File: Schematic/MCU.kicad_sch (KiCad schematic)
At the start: 21 parts, among them IC3 STM32H743VIT6, SW1 TS24CA, Y1 8MHz

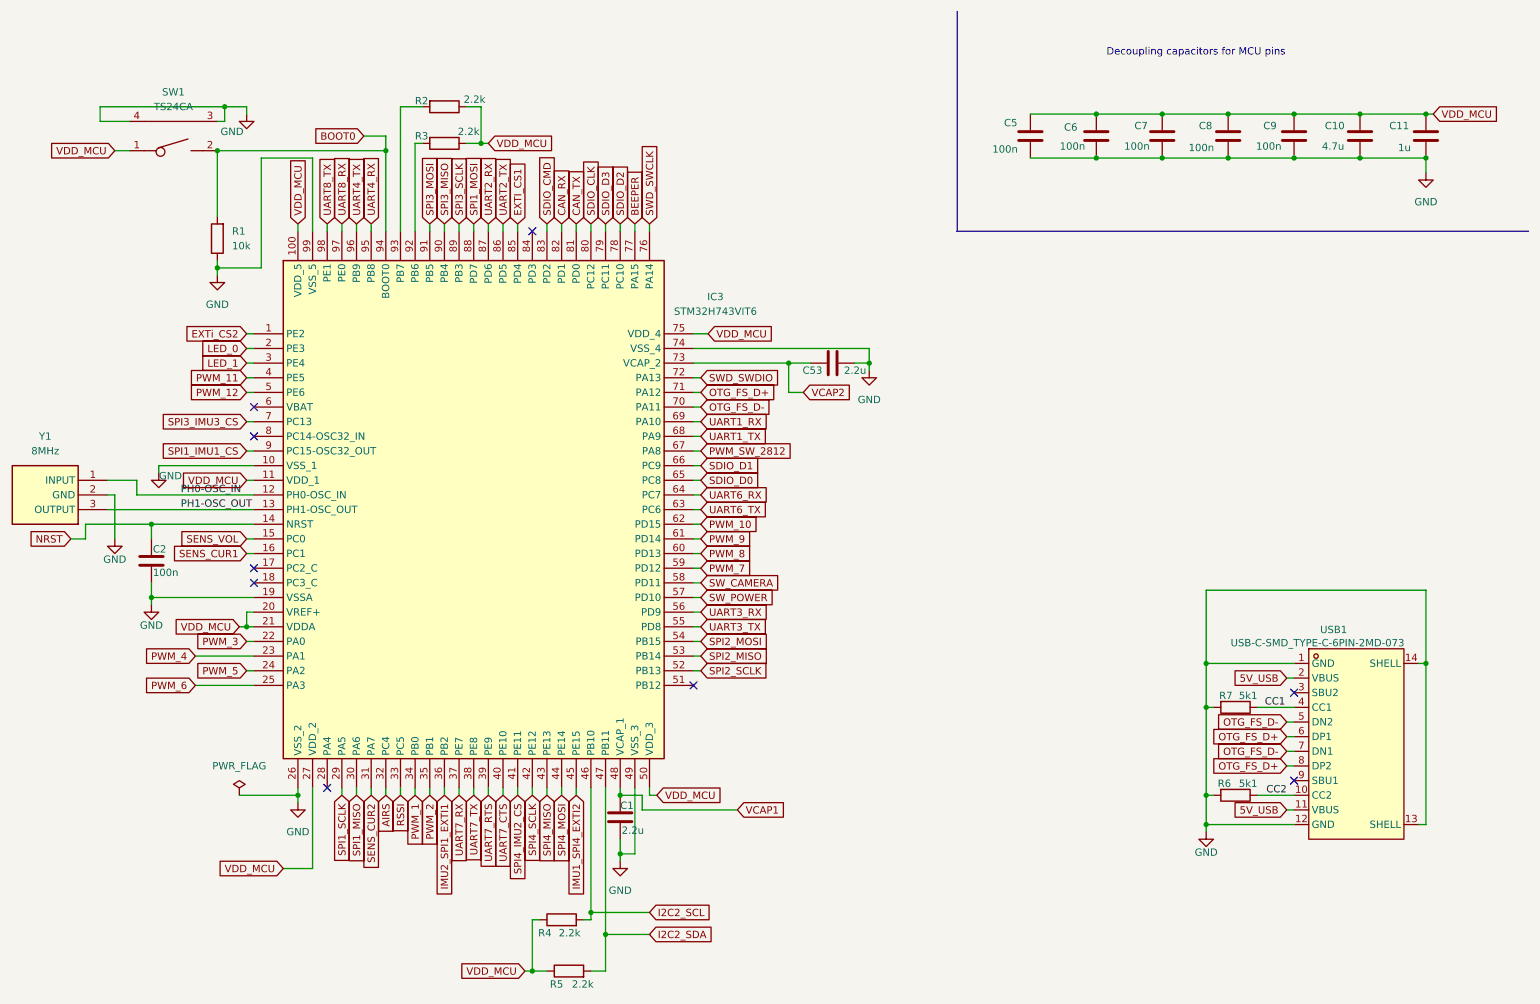
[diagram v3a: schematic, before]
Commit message: still routing and defining plan zones for power nets
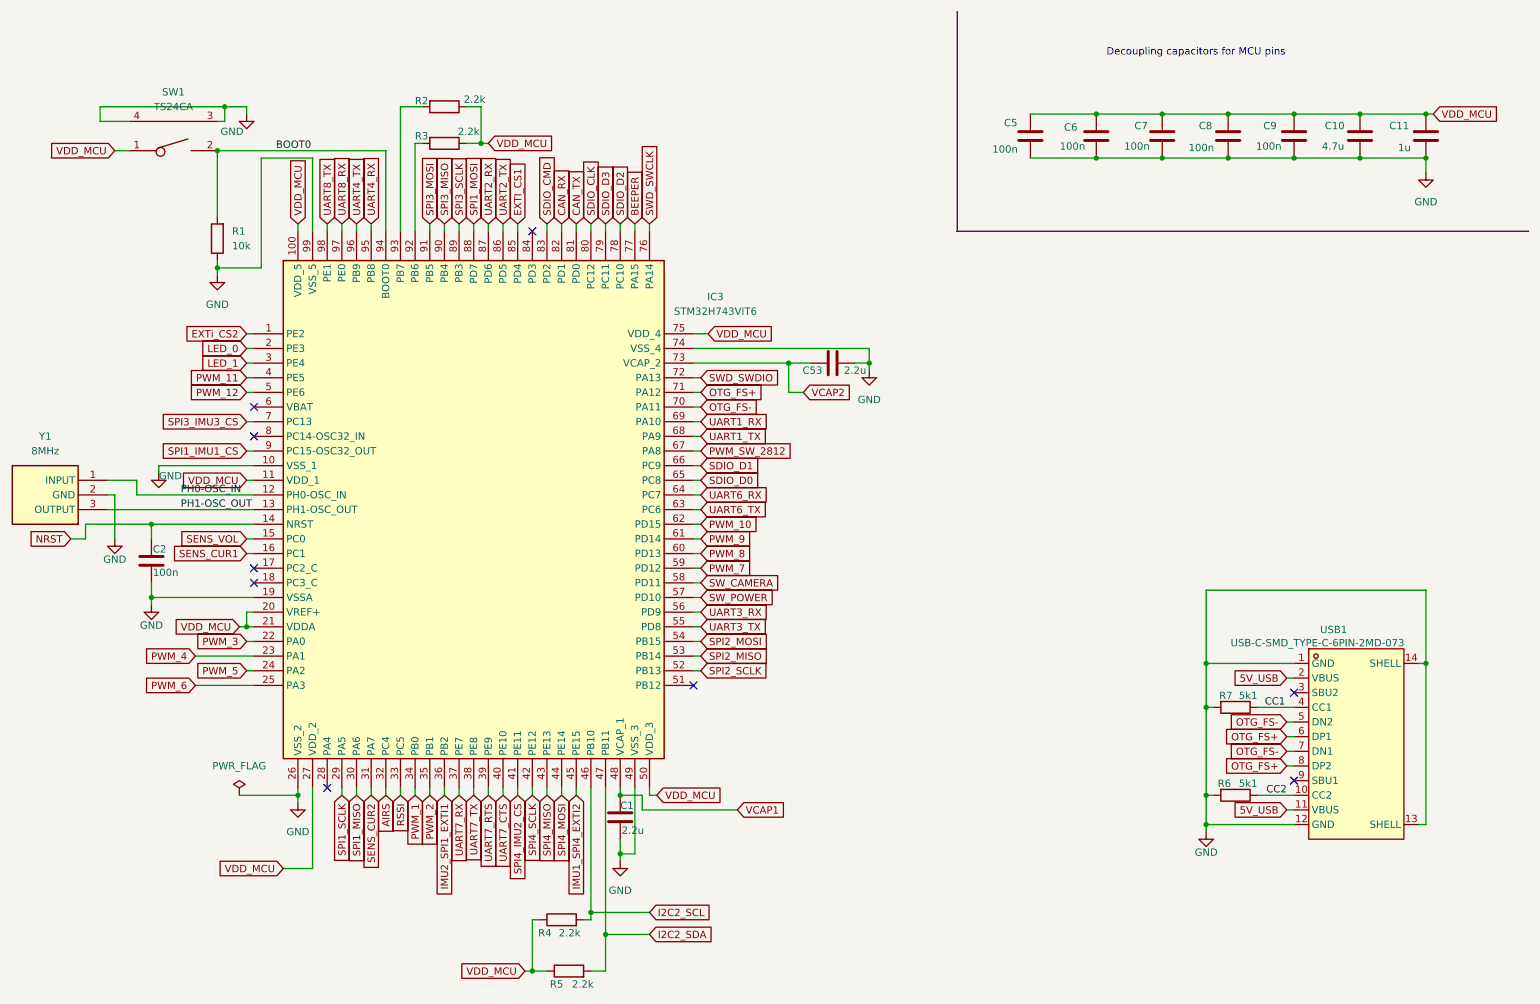
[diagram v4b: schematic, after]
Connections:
- net OTG_FS_D+ renamed OTG_FS+
- net OTG_FS_D- renamed OTG_FS-
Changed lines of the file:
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@@
 	)
 	(junction
-		(at 86.36 36.83)
-		(diameter 0)
-		(color 0 0 0 0)
-	)
-	(junction
 		(at 220.98 30.48)
 		(diameter 0)
@@
 	(wire
 		(pts
-			(xy 86.36 34.29) (xy 86.36 36.83)
-		)
-		(stroke
-			(width 0)
-			(type default)
-		)
-	)
-	(wire
-		(pts
 			(xy 242.57 135.89) (xy 243.84 135.89)
 		)
@@
 	(wire
 		(pts
-			(xy 82.55 34.29) (xy 86.36 34.29)
-		)
-		(stroke
-			(width 0)
-			(type default)
-		)
-	)
-	(wire
-		(pts
 			(xy 228.6 125.73) (xy 228.6 133.35)
 		)
@@
 		)
 	)
+	(label "BOOT0"
+		(at 67.31 36.83 0)
+		(effects
+			(font
+				(size 1.27 1.27)
+			)
+			(justify left bottom)
+		)
+	)
 	(label "PH1-OSC_OUT"
 		(at 50.8 99.06 0)
@@
 		)
 	)
-	(global_label "OTG_FS_D-"
+	(global_label "OTG_FS-"
 		(shape input)
 		(at 242.57 140.97 180)
@@
 		)
 		(property "Intersheetrefs" "${INTERSHEET_REFS}"
-			(at 228.941 140.97 0)
+			(at 231.1786 140.97 0)
 			(effects
 				(font
@@
 		)
 	)
-	(global_label "OTG_FS_D-"
+	(global_label "OTG_FS-"
 		(shape input)
 		(at 242.57 135.89 180)
@@
 		)
 		(property "Intersheetrefs" "${INTERSHEET_REFS}"
-			(at 228.941 135.89 0)
+			(at 231.1786 135.89 0)
 			(effects
 				(font
@@
 		)
 	)
-	(global_label "OTG_FS_D+"
+	(global_label "OTG_FS+"
 		(shape input)
 		(at 242.57 138.43 180)
@@
 		)
 		(property "Intersheetrefs" "${INTERSHEET_REFS}"
-			(at 228.941 138.43 0)
+			(at 231.1786 138.43 0)
 			(effects
 				(font
@@
 		)
 	)
-	(global_label "OTG_FS_D+"
+	(global_label "OTG_FS+"
 		(shape input)
 		(at 242.57 143.51 180)
@@
 		)
 		(property "Intersheetrefs" "${INTERSHEET_REFS}"
-			(at 228.941 143.51 0)
+			(at 231.1786 143.51 0)
 			(effects
 				(font
@@
 		)
 	)
-	(global_label "OTG_FS_D-"
+	(global_label "OTG_FS-"
 		(shape input)
 		(at 140.97 81.28 0)
@@
 		)
 		(property "Intersheetrefs" "${INTERSHEET_REFS}"
-			(at 154.599 81.28 0)
+			(at 152.3614 81.28 0)
 			(effects
 				(font
@@
 		)
 	)
-	(global_label "OTG_FS_D+"
+	(global_label "OTG_FS+"
 		(shape input)
 		(at 140.97 78.74 0)
@@
 		)
 		(property "Intersheetrefs" "${INTERSHEET_REFS}"
-			(at 154.599 78.74 0)
+			(at 152.3614 78.74 0)
 			(effects
 				(font
@@
 				(hide yes)
 			)
-		)
-	)
-	(global_label "BOOT0"
-		(shape input)
-		(at 82.55 34.29 180)
-		(fields_autoplaced yes)
-		(effects
-			(font
-				(size 1.27 1.27)
-			)
-			(justify right)
-		)
-		(property "Intersheetrefs" "${INTERSHEET_REFS}"
-			(at 73.4567 34.29 0)
-			(effects
-				(font
-					(size 1.27 1.27)
-				)
-				(justify right)
-				(hide yes)
-			)

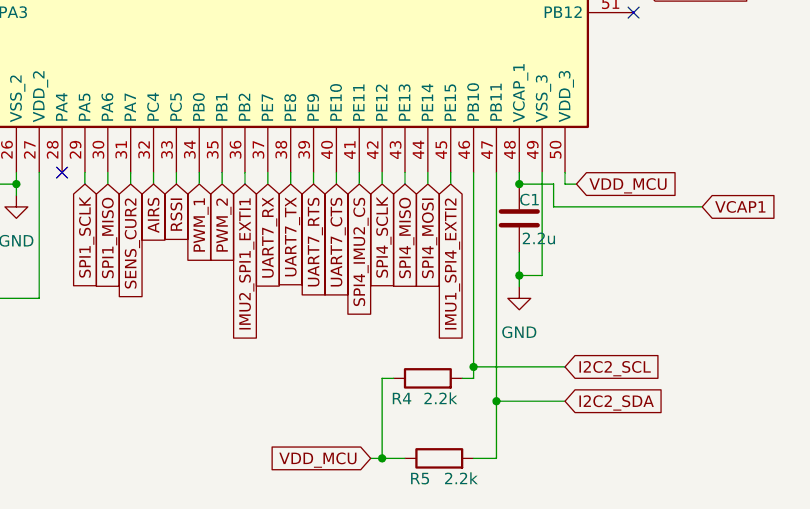
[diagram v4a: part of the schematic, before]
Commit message: Repositioned ICM for better routing, still MPU to place and route
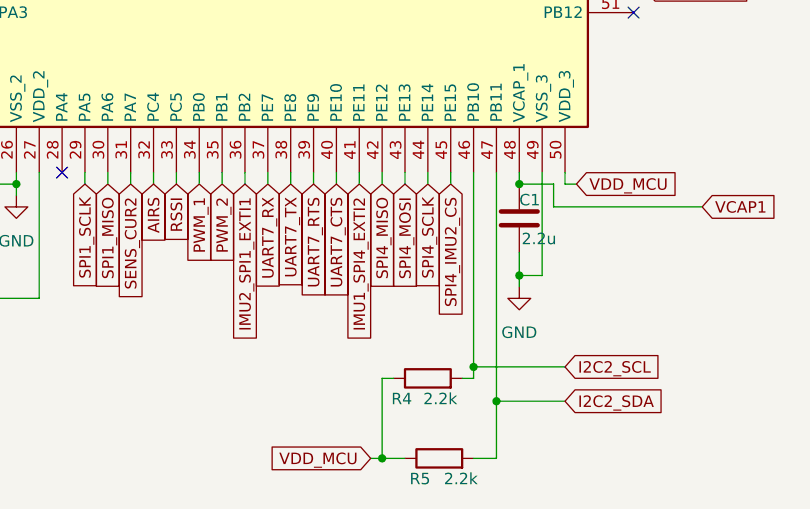
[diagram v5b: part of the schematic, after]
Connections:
- net IMU1_SPI4_EXTI2: now also IC3.41 (PE11); no longer IC3.45 (PE15)
- net SPI4_IMU2_CS: now also IC3.45 (PE15); no longer IC3.41 (PE11)
- net SPI4_MISO: now also IC3.42 (PE12); no longer IC3.43 (PE13)
- net SPI4_MOSI: now also IC3.43 (PE13); no longer IC3.44 (PE14)
- net SPI4_SCLK: now also IC3.44 (PE14); no longer IC3.42 (PE12)

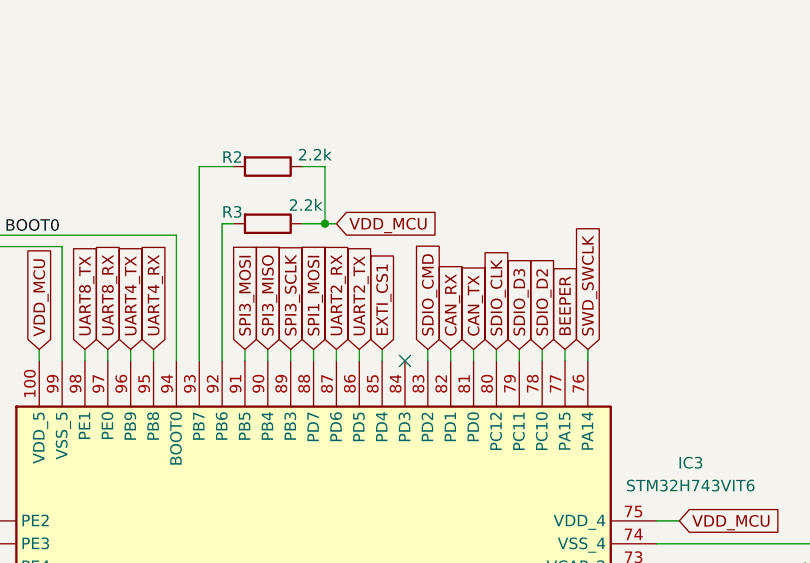
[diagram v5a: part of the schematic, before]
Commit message: finished every routing and fix errors in DRC
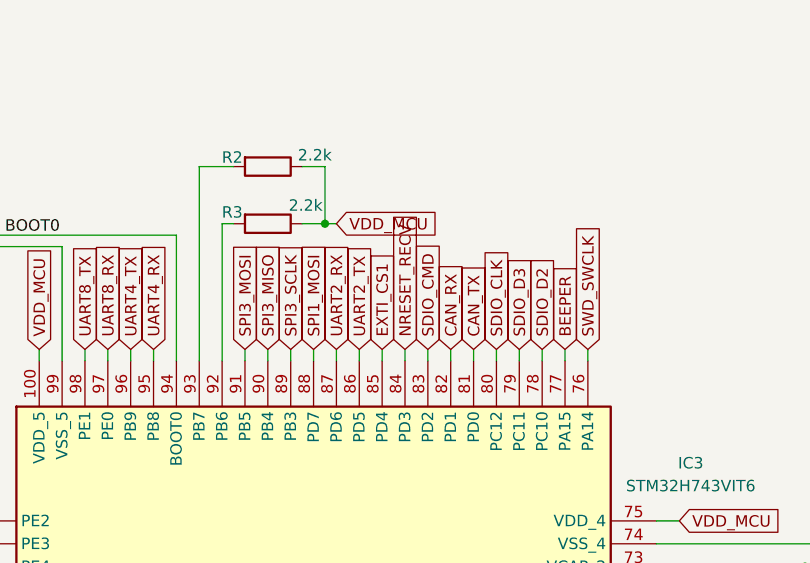
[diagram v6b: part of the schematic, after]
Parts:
- IC3: footprint fch7_fp:LQFP-100_14x14mm_P0.5mm_STM32H743 -> fch7:LQFP-100_14x14mm_P0.5mm_STM32H743
- SW1: footprint fch7_fp:SW-SMD_2P-TS24CA -> fch7:SW-SMD_2P-TS24CA
- USB1: footprint fch7_fp:USB-C-SMD_TYPE-C-6PIN-2MD-073 -> fch7:USB-C-SMD_TYPE-C-6PIN-2MD-073
- Y1: footprint fch7_fp:CSTNE8M00G55Z000R0 -> fch7:CSTNE8M00G55Z000R0
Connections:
- net NRESET_RECV: now reaches IC3.84 (PD3)
- no-connect marks 9 -> 8
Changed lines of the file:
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@@
 	)
 	(no_connect
-		(at 111.76 50.8)
-	)
-	(no_connect
 		(at 63.5 81.28)
 	)
@@
 	(wire
 		(pts
+			(xy 111.76 49.53) (xy 111.76 50.8)
+		)
+		(stroke
+			(width 0)
+			(type default)
+		)
+	)
+	(wire
+		(pts
 			(xy 121.92 168.91) (xy 121.92 170.18)
 		)
@@
 		)
 	)
+	(global_label "NRESET_RECV"
+		(shape input)
+		(at 111.76 49.53 90)
+		(fields_autoplaced yes)
+		(effects
+			(font
+				(size 1.27 1.27)
+			)
+			(justify left)
+		)
+		(property "Intersheetrefs" "${INTERSHEET_REFS}"
+			(at 111.76 33.724 90)
+			(effects
+				(font
+					(size 1.27 1.27)
+				)
+				(justify left)
+				(hide yes)
+			)
+		)
+	)
 	(global_label "PWM_7"
 		(shape input)
@@
 			)
 		)
-		(property "Footprint" "fch7_fp:USB-C-SMD_TYPE-C-6PIN-2MD-073"
+		(property "Footprint" "fch7:USB-C-SMD_TYPE-C-6PIN-2MD-073"
 			(at 254 162.56 0)
 			(effects
@@
 			)
 		)
-		(property "Footprint" "fch7_fp:SW-SMD_2P-TS24CA"
+		(property "Footprint" "fch7:SW-SMD_2P-TS24CA"
 			(at 48.768 27.686 0)
 			(effects
@@
 			)
 		)
-		(property "Footprint" "fch7_fp:CSTNE8M00G55Z000R0"
+		(property "Footprint" "fch7:CSTNE8M00G55Z000R0"
 			(at 16.51 4.14 0)
 			(effects
@@
 			)
 		)
-		(property "Footprint" "fch7_fp:LQFP-100_14x14mm_P0.5mm_STM32H743"
+		(property "Footprint" "fch7:LQFP-100_14x14mm_P0.5mm_STM32H743"
 			(at 135.89 153.34 0)
 			(effects

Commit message: Update schematic properties and model paths - Added MPN and Manufacturer properties for ICM-42688-P and MPU-6500 in sensors.kicad_sch. - Changed model paths to use the ${FCH7_3DMODEL_DIR} variable for various components in the fch7.pretty library. - Added a 3D model for the SOD-123 component.
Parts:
- IC3: MPN (none) -> STM32H743VIT6; Manufacturer (none) -> STM
- USB1: MPN (none) -> TYPE-C 16PIN 2MD(073)
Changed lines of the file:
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@@
+			)
+		)
+		(property "MPN" "TYPE-C 16PIN 2MD(073)"
+			(at 255.27 139.7 0)
+			(effects
+				(font
+					(size 1.27 1.27)
+				)
+				(hide yes)
 			)
 		)
@@
 				(hide yes)
 			)
+		)
+		(property "MPN" "STM32H743VIT6"
+			(at 63.5 68.58 0)
+			(effects
+				(font
+					(size 1.27 1.27)
+				)
+				(hide yes)
+			)
+		)
+		(property "Manufacturer" "STM"
+			(at 63.5 68.58 0)
+			(effects
+				(font
+					(size 1.27 1.27)
+				)
+				(hide yes)
+			)
